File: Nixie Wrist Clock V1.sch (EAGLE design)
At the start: 39 parts, among them Q1 310mA/60V/1.6Ω, Q2 310mA/60V/1.6Ω, Q3 310mA/60V/1.6Ω, Q4 310mA/60V/1.6Ω, Q5 310mA/60V/1.6Ω, U2 NRF52832, X3 32MHz, X4 32.768kHz

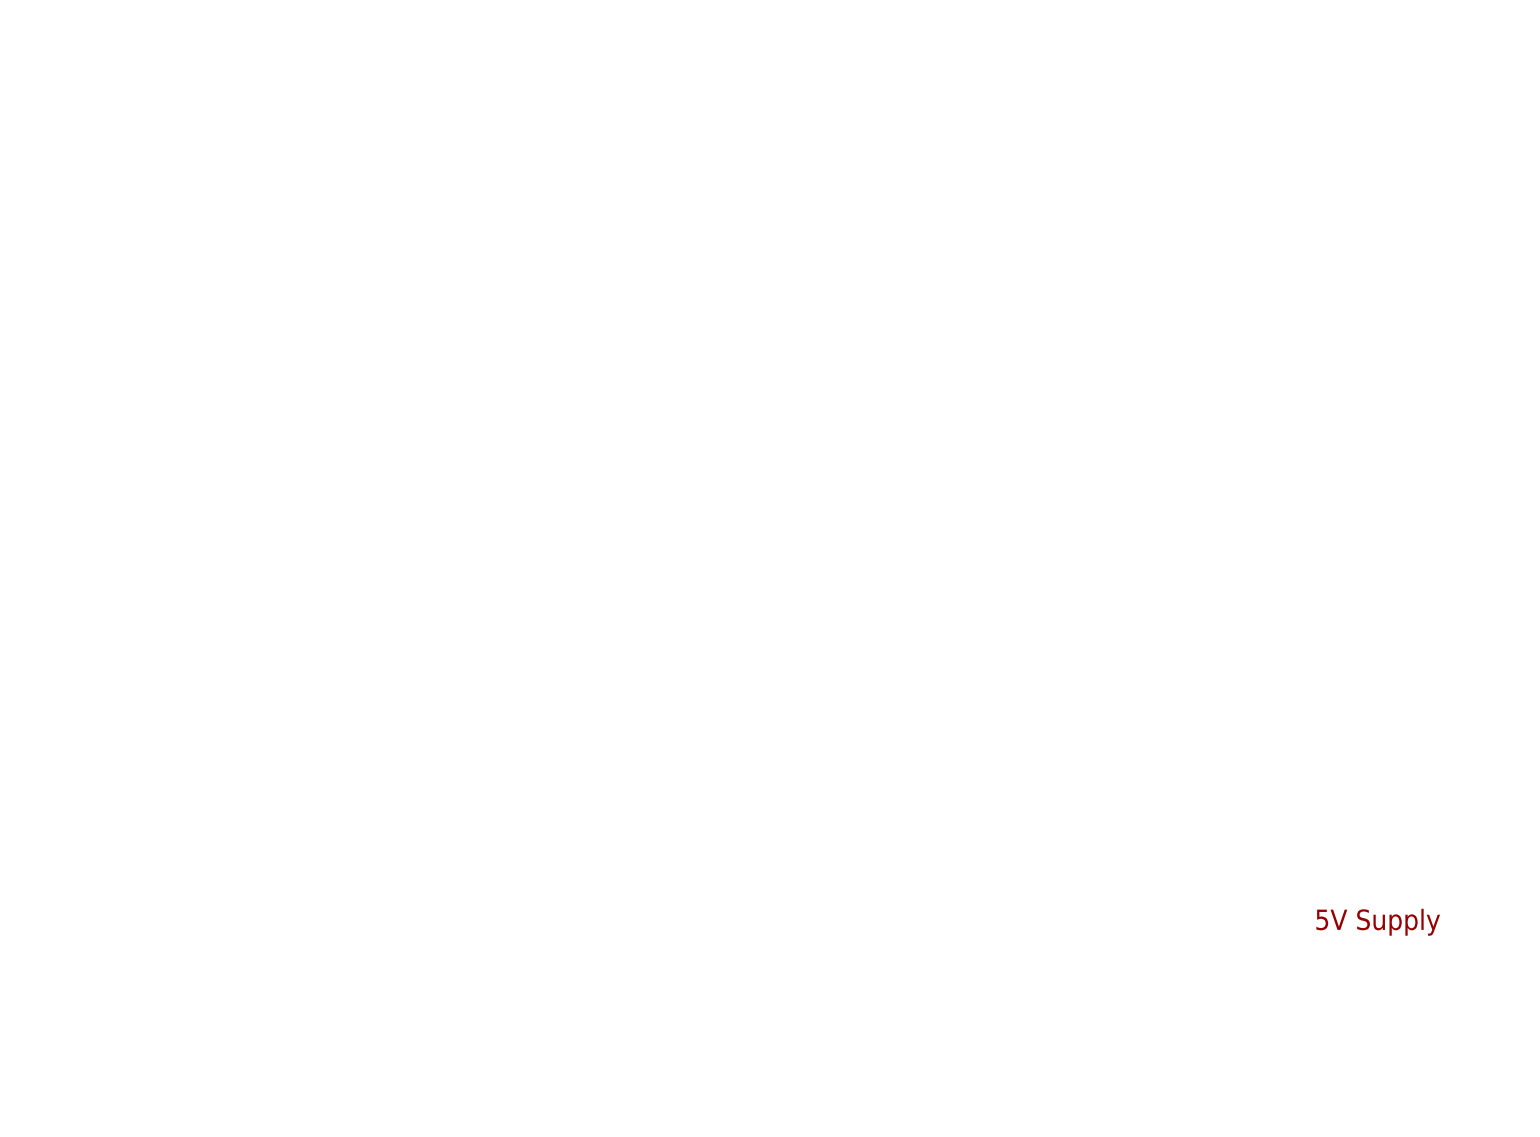
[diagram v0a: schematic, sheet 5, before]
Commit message: Update #6
5V Supply IC added
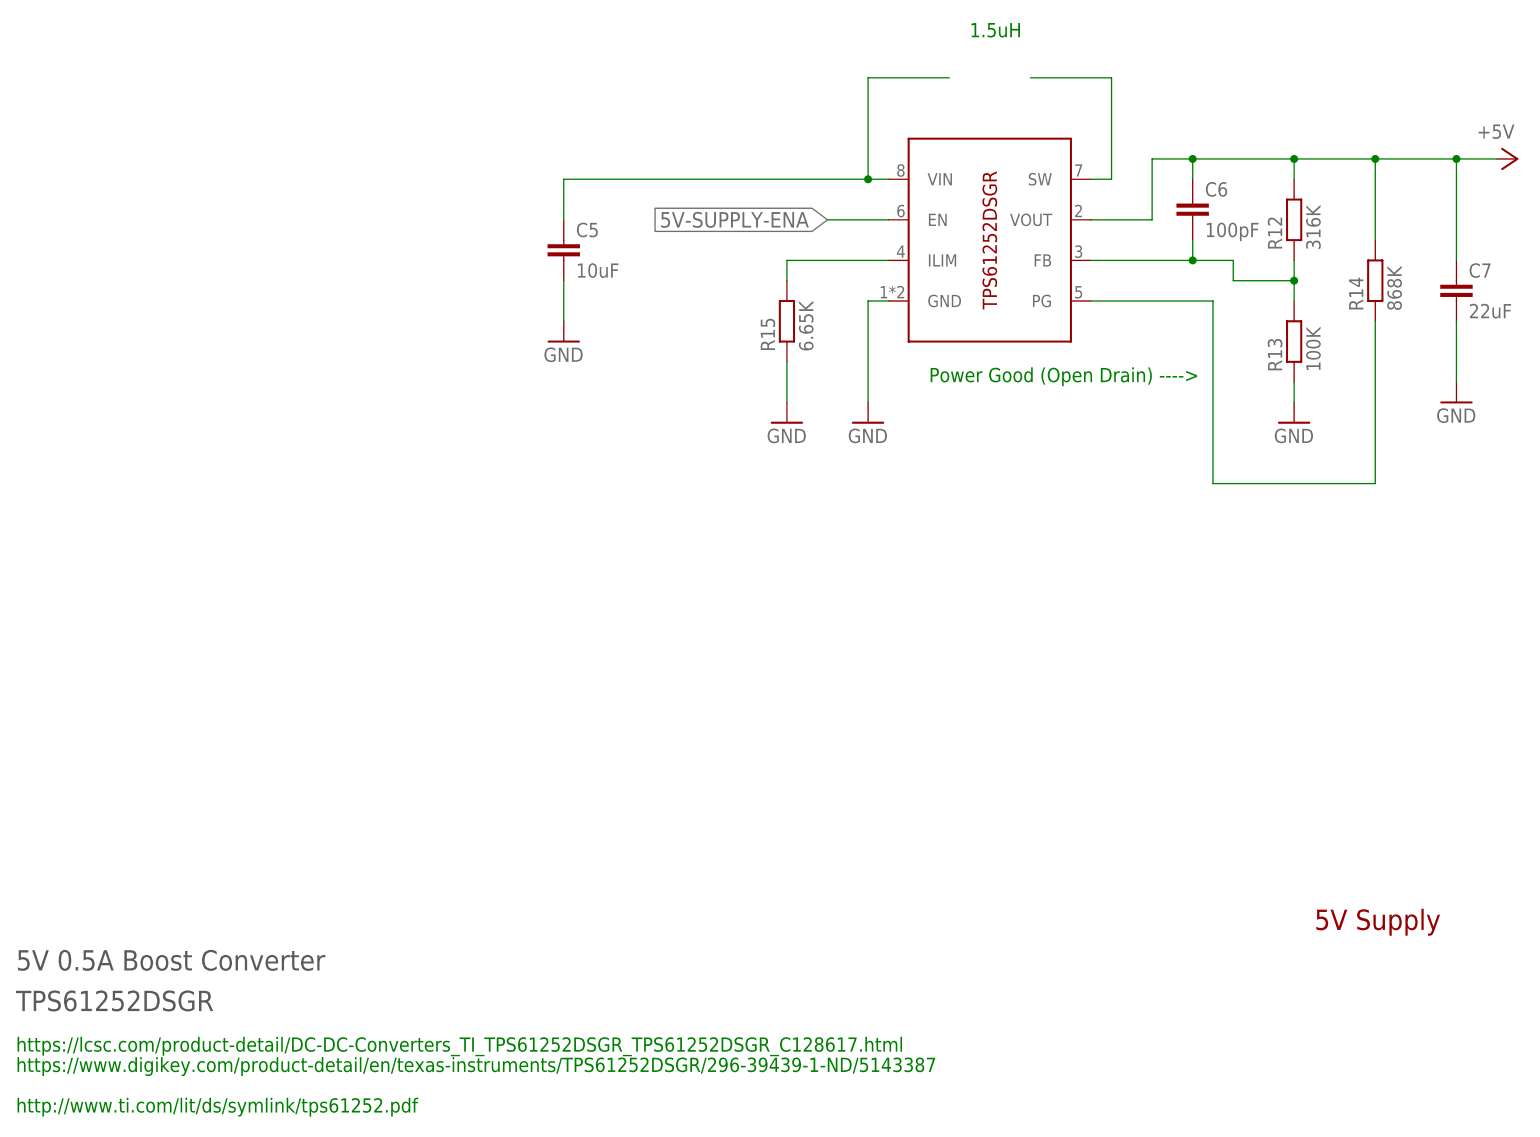
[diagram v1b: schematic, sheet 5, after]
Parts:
- added C5: 10uF, rcl:C-EUC0805
- added C6: 100pF, rcl:C-EUC0805
- added C7: 22uF, rcl:C-EUC0805
- added R12: 316K, rcl:R-EU_R0805
- added R13: 100K, rcl:R-EU_R0805
- added R14: 868K, rcl:R-EU_R0805
- added R15: 6.65K, rcl:R-EU_R0805
- added U$4: TPS61252DSGR, Alp-Special:TPS61252DSGR
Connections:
- new net 5V-SUPPLY-ENA: U$4.EN
- new net N$10: R14.1, U$4.PG
- new net N$12: C5.1, U$4.VIN
- new net N$13: U$4.SW
- new net N$15: C6.2, R12.1, R13.2, U$4.FB
- new net N$2: R15.2, U$4.ILIM
- net +5V: now also C6.1, C7.1, R12.2, R14.2, U$4.VOUT
- net GND: now also C5.2, C7.2, R13.1, R15.1, U$4.GND
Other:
- note added: "1.5uH"
- note added: "5V 0.5A Boost Converter"
- note added: "LiPo Charger"
- note added: "Power Good (Open Drain) ---->"
- note added: "TPS61252DSGR"
- note added: "http://www.ti.com/lit/ds/symlink/tps61252.pdf"
- note added: "https://lcsc.com/product-detail/DC-DC-Converters_TI_TPS61252DSGR_TPS61252DSGR_C128617.html"
- note added: "https://www.digikey.com/product-detail/en/texas-instruments/TPS61252DSGR/296-39439-1-ND/5143387"

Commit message: Revert "Update #6"
This reverts commit 39989620e637334a808b500ab2563335b83f3b38.
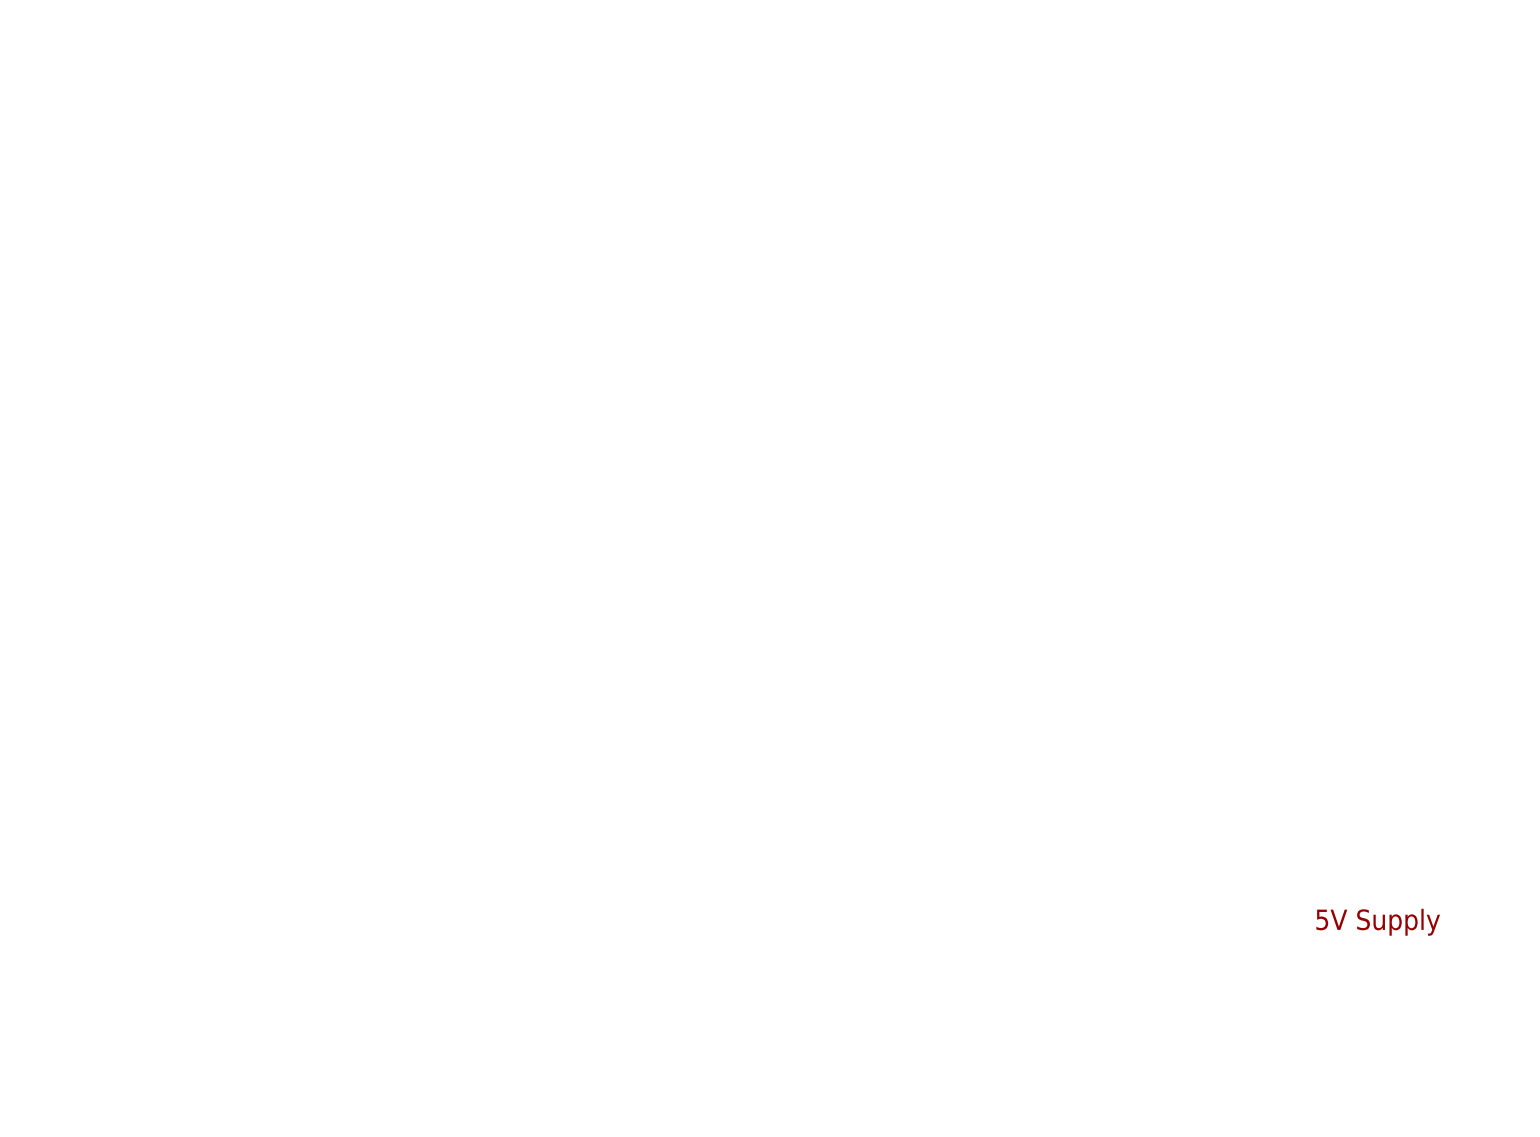
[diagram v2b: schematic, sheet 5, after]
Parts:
- removed C5: 10uF, rcl:C-EUC0805
- removed C6: 100pF, rcl:C-EUC0805
- removed C7: 22uF, rcl:C-EUC0805
- removed R12: 316K, rcl:R-EU_R0805
- removed R13: 100K, rcl:R-EU_R0805
- removed R14: 868K, rcl:R-EU_R0805
- removed R15: 6.65K, rcl:R-EU_R0805
- removed U$4: TPS61252DSGR, Alp-Special:TPS61252DSGR
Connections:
- removed net 5V-SUPPLY-ENA: U$4.EN
- removed net N$10: R14.1, U$4.PG
- removed net N$12: C5.1, U$4.VIN
- removed net N$13: U$4.SW
- removed net N$15: C6.2, R12.1, R13.2, U$4.FB
- removed net N$2: R15.2, U$4.ILIM
- net +5V: no longer C6.1, C7.1, R12.2, R14.2, U$4.VOUT
- net GND: no longer C5.2, C7.2, R13.1, R15.1, U$4.GND
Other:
- note removed: "1.5uH"
- note removed: "5V 0.5A Boost Converter"
- note removed: "LiPo Charger"
- note removed: "Power Good (Open Drain) ---->"
- note removed: "TPS61252DSGR"
- note removed: "http://www.ti.com/lit/ds/symlink/tps61252.pdf"
- note removed: "https://lcsc.com/product-detail/DC-DC-Converters_TI_TPS61252DSGR_TPS61252DSGR_C128617.html"
- note removed: "https://www.digikey.com/product-detail/en/texas-instruments/TPS61252DSGR/296-39439-1-ND/5143387"
